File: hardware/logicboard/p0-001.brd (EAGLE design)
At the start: 91 x 57 mm, 23 parts, among them IC1 74ALS05N, IC2 LTC485N, IC3 LTC485N, J1 DIN5, J2 DIN5, J3 DIN5, X1 NELTRON-7810-XPXC, X2 NELTRON-7810-XPXC

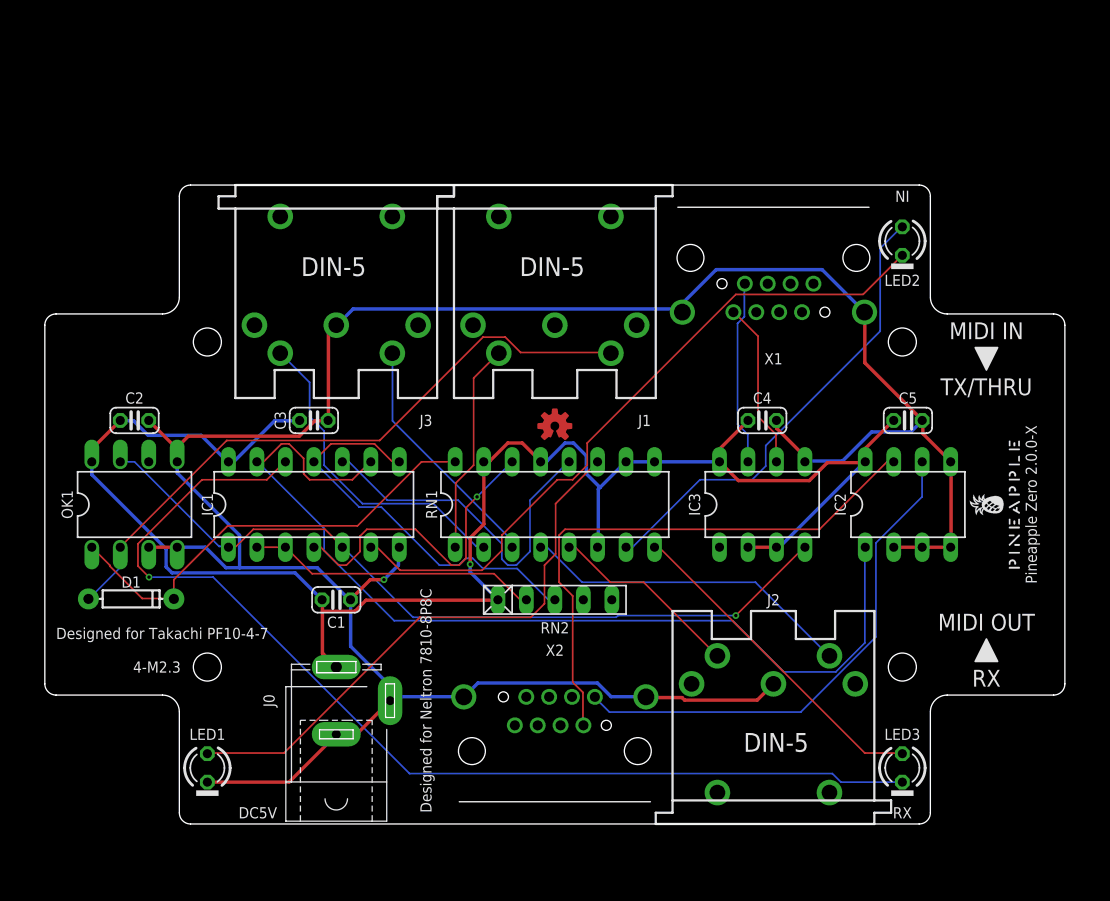
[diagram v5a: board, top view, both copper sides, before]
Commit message: Swapped IC2 and IC3.
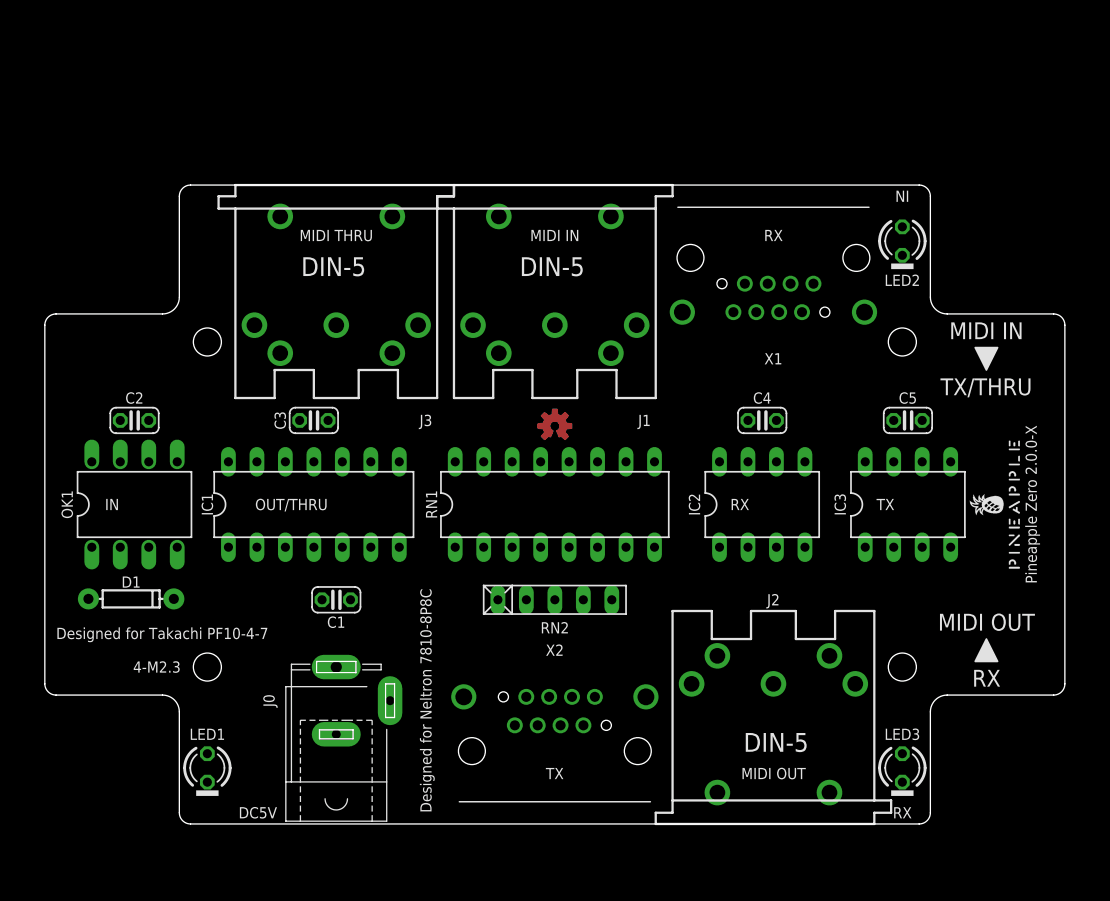
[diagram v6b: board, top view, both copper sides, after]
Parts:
- moved IC2 13.0 mm to (64.0, 28.5)
- moved IC3 13.0 mm to (77.0, 28.5)
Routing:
- net GND: track 231.9 -> 0.00 mm, vias 1 -> 0
- net VCC: track 157.1 -> 0.00 mm, vias 1 -> 0
- net N$15: track 94.3 -> 0.00 mm, vias 1 -> 0
- net MIDIOUT: track 86.4 -> 0.00 mm
- net N$3: track 70.8 -> 0.00 mm, vias 1 -> 0
- net N$2: track 61.9 -> 0.00 mm
- net MIDIIN-: track 58.0 -> 0.00 mm
- net RX-: track 50.4 -> 0.00 mm
- net N$12: track 50.2 -> 0.00 mm
- net RX+: track 45.8 -> 0.00 mm
- net N$13: track 41.9 -> 0.00 mm
- net MIDIINA: track 40.5 -> 0.00 mm
- net N$11: track 36.1 -> 0.00 mm
- net N$10: track 31.3 -> 0.00 mm
- net N$8: track 29.8 -> 0.00 mm
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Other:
- board text added: "MIDI THRU"
- board text added: "OUT/THRU"

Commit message: Rearranged connectors.
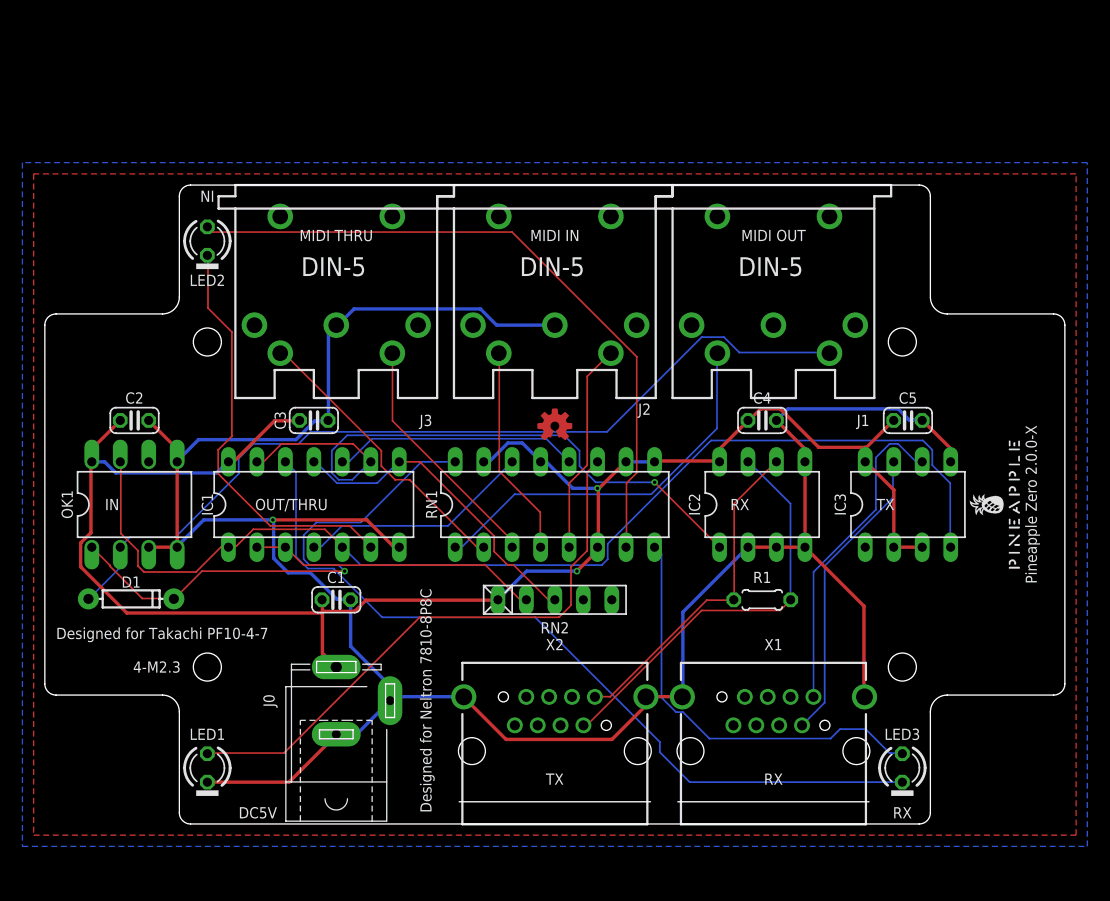
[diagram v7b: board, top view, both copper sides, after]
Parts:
- added R1: (no value), rcl:0204/5
- moved LED2 62.0 mm to (14.5, 52.0)
- moved J2 60.2 mm to (45.5, 57.0), turned to 180 degrees
- moved X1 44.0 mm to (65.0, 6.50), turned to 180 degrees
- moved J1 19.5 mm to (65.0, 57.0)
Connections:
- net RX+: now also R1.1
- net RX-: now also R1.2
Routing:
- net GND: track 0.00 -> 220.3 mm, vias 0 -> 1
- net VCC: track 0.00 -> 156.4 mm, vias 0 -> 2
- net N$3: track 0.00 -> 99.2 mm
- net MIDIIN-: track 0.00 -> 78.3 mm
- net N$15: track 0.00 -> 71.8 mm
- net N$13: track 0.00 -> 60.5 mm
- net MIDIOUT: track 0.00 -> 58.0 mm, vias 0 -> 1
- net N$12: track 0.00 -> 51.7 mm
- net MIDIINA: track 0.00 -> 48.0 mm, vias 0 -> 1
- net N$14: track 0.00 -> 37.9 mm
- net N$2: track 0.00 -> 37.2 mm
- net RX-: track 0.00 -> 37.1 mm
- net N$1: track 0.00 -> 34.5 mm
- net RX+: track 0.00 -> 29.9 mm
- net N$11: track 0.00 -> 29.0 mm
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- added copper zone on layer 1, net GND
- added copper zone on layer 16, net GND
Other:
- board text removed: "TX/THRU"

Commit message: Added values of components.
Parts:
- C1: value (none) -> 100n
- C2, C3, C4, C5: value (none) -> 10n
- J0: value (none) -> DC5V
- LED1: value (none) -> GREEN
- LED2: value (none) -> RED
- LED3: value (none) -> YELLOW
- R1: value (none) -> 100
- RN1: value (none) -> 220
- RN2: value (none) -> 4.7k
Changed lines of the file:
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@@
 <attribute name="VALUE" x="46.77" y="53.063" size="0.6096" layer="27" font="vector" ratio="20" rot="R180"/>
 </element>
-<element name="J0" library="con-jack" library_urn="urn:adsk.eagle:library:154" package="SPC4077" package3d_urn="urn:adsk.eagle:package:7492/1" value="" x="26" y="11" smashed="yes" rot="R90">
+<element name="J0" library="con-jack" library_urn="urn:adsk.eagle:library:154" package="SPC4077" package3d_urn="urn:adsk.eagle:package:7492/1" value="DC5V" x="26" y="11" smashed="yes" rot="R90">
 <attribute name="MF" value="" x="26" y="11" size="1.778" layer="27" rot="R90" display="off"/>
 <attribute name="MPN" value="" x="26" y="11" size="1.778" layer="27" rot="R90" display="off"/>
@@
 <attribute name="VALUE" x="17.269" y="27.865" size="1.27" layer="27" ratio="10"/>
 </element>
-<element name="RN1" library="resistor-dil" library_urn="urn:adsk.eagle:library:342" package="DIL16" package3d_urn="urn:adsk.eagle:package:922/2" value="" x="45.5" y="28.5" smashed="yes">
+<element name="RN1" library="resistor-dil" library_urn="urn:adsk.eagle:library:342" package="DIL16" package3d_urn="urn:adsk.eagle:package:922/2" value="220" x="45.5" y="28.5" smashed="yes">
 <attribute name="MF" value="" x="45.5" y="28.5" size="1.778" layer="27" display="off"/>
 <attribute name="MPN" value="" x="45.5" y="28.5" size="1.778" layer="27" display="off"/>
@@
 <attribute name="VALUE" x="38.007" y="27.865" size="1.27" layer="27" ratio="10"/>
 </element>
-<element name="RN2" library="resistor-net" library_urn="urn:adsk.eagle:library:343" package="RN-5" package3d_urn="urn:adsk.eagle:package:24976/1" value="" x="45.5" y="20" smashed="yes">
+<element name="RN2" library="resistor-net" library_urn="urn:adsk.eagle:library:343" package="RN-5" package3d_urn="urn:adsk.eagle:package:24976/1" value="4.7k" x="45.5" y="20" smashed="yes">
 <attribute name="MF" value="" x="45.5" y="20" size="1.778" layer="27" display="off"/>
 <attribute name="MPN" value="" x="45.5" y="20" size="1.778" layer="27" display="off"/>
@@
 <attribute name="VALUE" x="41.69" y="17.079" size="1.27" layer="27" ratio="10"/>
 </element>
-<element name="C1" library="rcl" library_urn="urn:adsk.eagle:library:334" package="C025-024X044" package3d_urn="urn:adsk.eagle:package:23630/1" value="" x="26" y="20" smashed="yes">
+<element name="C1" library="rcl" library_urn="urn:adsk.eagle:library:334" package="C025-024X044" package3d_urn="urn:adsk.eagle:package:23630/1" value="100n" x="26" y="20" smashed="yes">
 <attribute name="NAME" x="26" y="22" size="1" layer="25" ratio="10" align="center"/>
 <attribute name="POPULARITY" value="56" x="26" y="20" size="1.778" layer="27" display="off"/>
@@
 <attribute name="VALUE" x="24.222" y="17.333" size="1.27" layer="27" ratio="10"/>
 </element>
-<element name="C2" library="rcl" library_urn="urn:adsk.eagle:library:334" package="C025-024X044" package3d_urn="urn:adsk.eagle:package:23630/1" value="" x="8" y="36" smashed="yes">
+<element name="C2" library="rcl" library_urn="urn:adsk.eagle:library:334" package="C025-024X044" package3d_urn="urn:adsk.eagle:package:23630/1" value="10n" x="8" y="36" smashed="yes">
 <attribute name="NAME" x="8" y="38" size="1" layer="25" ratio="10" align="center"/>
 <attribute name="POPULARITY" value="56" x="8" y="36" size="1.778" layer="27" display="off"/>
@@
 <attribute name="VALUE" x="6.222" y="33.333" size="1.27" layer="27" ratio="10"/>
 </element>
-<element name="C3" library="rcl" library_urn="urn:adsk.eagle:library:334" package="C025-024X044" package3d_urn="urn:adsk.eagle:package:23630/1" value="" x="24" y="36" smashed="yes">
+<element name="C3" library="rcl" library_urn="urn:adsk.eagle:library:334" package="C025-024X044" package3d_urn="urn:adsk.eagle:package:23630/1" value="10n" x="24" y="36" smashed="yes">
 <attribute name="NAME" x="21" y="36" size="1" layer="25" ratio="10" rot="R90" align="center"/>
 <attribute name="POPULARITY" value="56" x="24" y="36" size="1.778" layer="27" display="off"/>
@@
 <attribute name="VALUE" x="22.222" y="33.333" size="1.27" layer="27" ratio="10"/>
 </element>
-<element name="C4" library="rcl" library_urn="urn:adsk.eagle:library:334" package="C025-024X044" package3d_urn="urn:adsk.eagle:package:23630/1" value="" x="64" y="36" smashed="yes">
+<element name="C4" library="rcl" library_urn="urn:adsk.eagle:library:334" package="C025-024X044" package3d_urn="urn:adsk.eagle:package:23630/1" value="10n" x="64" y="36" smashed="yes">
 <attribute name="NAME" x="64" y="38" size="1" layer="25" ratio="10" align="center"/>
 <attribute name="POPULARITY" value="56" x="64" y="36" size="1.778" layer="27" display="off"/>
@@
 <attribute name="VALUE" x="62.222" y="33.333" size="1.27" layer="27" ratio="10"/>
 </element>
-<element name="C5" library="rcl" library_urn="urn:adsk.eagle:library:334" package="C025-024X044" package3d_urn="urn:adsk.eagle:package:23630/1" value="" x="77" y="36" smashed="yes">
+<element name="C5" library="rcl" library_urn="urn:adsk.eagle:library:334" package="C025-024X044" package3d_urn="urn:adsk.eagle:package:23630/1" value="10n" x="77" y="36" smashed="yes">
 <attribute name="NAME" x="77" y="38" size="1" layer="25" ratio="10" align="center"/>
 <attribute name="POPULARITY" value="56" x="77" y="36" size="1.778" layer="27" display="off"/>
@@
 <attribute name="VALUE" x="75.222" y="33.333" size="1.27" layer="27" ratio="10"/>
 </element>
-<element name="LED1" library="led" library_urn="urn:adsk.eagle:library:259" package="LED3MM" package3d_urn="urn:adsk.eagle:package:15797/1" value="" x="14.5" y="5" smashed="yes" rot="R270">
+<element name="LED1" library="led" library_urn="urn:adsk.eagle:library:259" package="LED3MM" package3d_urn="urn:adsk.eagle:package:15797/1" value="GREEN" x="14.5" y="5" smashed="yes" rot="R270">
 <attribute name="NAME" x="14.5" y="8" size="1" layer="25" ratio="10" align="center"/>
 <attribute name="POPULARITY" value="97" x="14.5" y="5" size="1.778" layer="27" rot="R270" display="off"/>
 <attribute name="VALUE" x="12.849" y="3.095" size="1.27" layer="27" ratio="10" rot="R270"/>
 </element>
-<element name="LED2" library="led" library_urn="urn:adsk.eagle:library:259" package="LED3MM" package3d_urn="urn:adsk.eagle:package:15797/1" value="" x="14.5" y="52" smashed="yes" rot="R270">
+<element name="LED2" library="led" library_urn="urn:adsk.eagle:library:259" package="LED3MM" package3d_urn="urn:adsk.eagle:package:15797/1" value="RED" x="14.5" y="52" smashed="yes" rot="R270">
 <attribute name="NAME" x="14.5" y="48.5" size="1" layer="25" ratio="10" align="center"/>
 <attribute name="POPULARITY" value="97" x="14.5" y="52" size="1.778" layer="27" rot="R270" display="off"/>
 <attribute name="VALUE" x="12.849" y="50.095" size="1.27" layer="27" ratio="10" rot="R270"/>
 </element>
-<element name="LED3" library="led" library_urn="urn:adsk.eagle:library:259" package="LED3MM" package3d_urn="urn:adsk.eagle:package:15797/1" value="" x="76.5" y="5" smashed="yes" rot="R270">
+<element name="LED3" library="led" library_urn="urn:adsk.eagle:library:259" package="LED3MM" package3d_urn="urn:adsk.eagle:package:15797/1" value="YELLOW" x="76.5" y="5" smashed="yes" rot="R270">
 <attribute name="NAME" x="76.5" y="8" size="1" layer="25" ratio="10" align="center"/>
 <attribute name="POPULARITY" value="97" x="76.5" y="5" size="1.778" layer="27" rot="R270" display="off"/>
 <attribute name="VALUE" x="74.849" y="3.095" size="1.27" layer="27" ratio="10" rot="R270"/>
 </element>
-<element name="R1" library="rcl" library_urn="urn:adsk.eagle:library:334" package="0204/5" package3d_urn="urn:adsk.eagle:package:23488/1" value="" x="64" y="20" smashed="yes">
+<element name="R1" library="rcl" library_urn="urn:adsk.eagle:library:334" package="0204/5" package3d_urn="urn:adsk.eagle:package:23488/1" value="100" x="64" y="20" smashed="yes">
 <attribute name="NAME" x="64" y="22" size="1" layer="25" ratio="10" align="center"/>
 <attribute name="POPULARITY" value="35" x="64" y="20" size="1.778" layer="27" display="off"/>
